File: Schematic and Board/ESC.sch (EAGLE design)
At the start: 45 parts

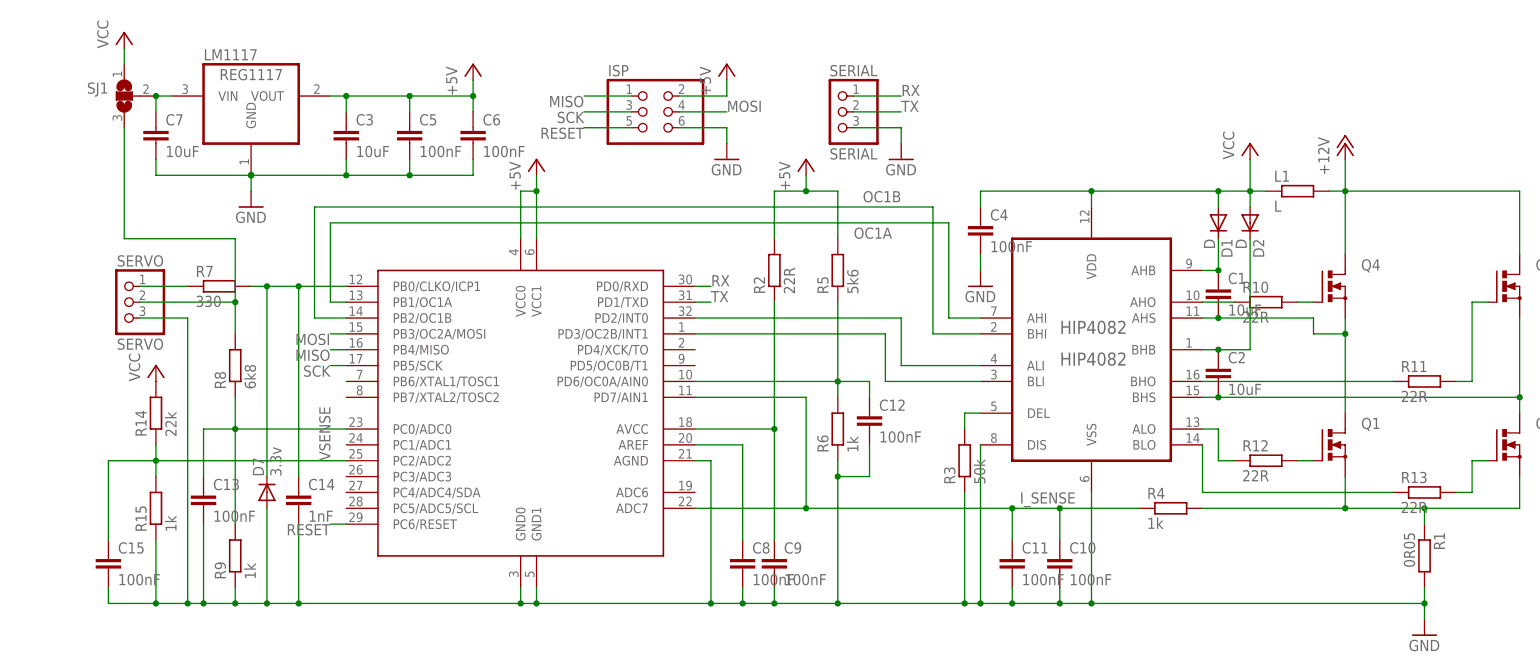
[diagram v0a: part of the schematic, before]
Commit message: updated board: makes better use of PWM outputs, also adds optional ACS712 hall effect current sensor
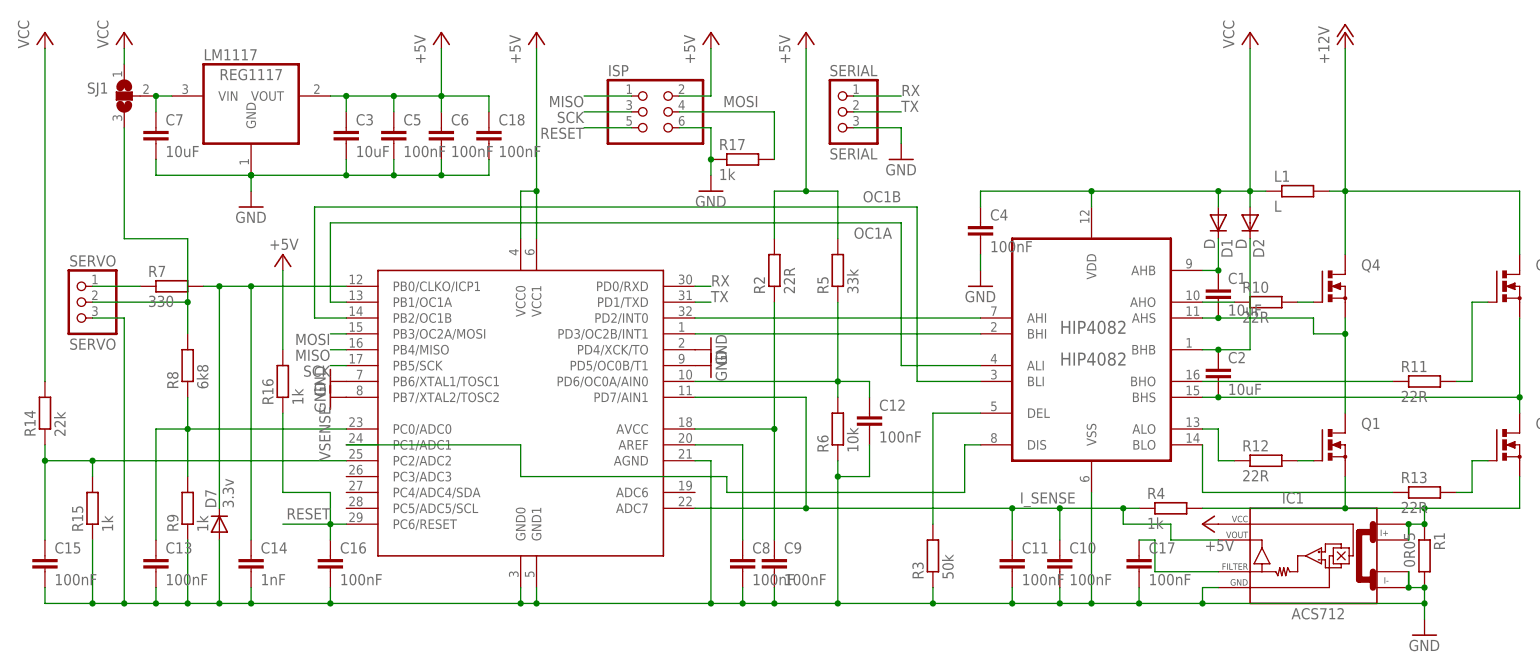
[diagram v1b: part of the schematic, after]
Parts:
- added C16, C17, C18: 100nF, rcl:C-EUC0603K
- added IC1: ACS712, ACS712:ACS712
- added R16, R17: 1k, rcl:R-EU_R0603
- R2, R3, R4, R8, R9: device rcl:R-EU_R0805 -> rcl:R-EU_R0603
- R5: value 5k6 -> 33k; device rcl:R-EU_R0805 -> rcl:R-EU_R0603
- R6: value 1k -> 10k; device rcl:R-EU_R0805 -> rcl:R-EU_R0603
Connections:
- new net AHI: ATMEGA328.PD2/INT0, HIP4082.AHI
- new net BHI: ATMEGA328.PD3/OC2B/INT1, HIP4082.BHI
- net +5V: now also C18.1, IC1.VCC, R16.2
- net GND: now also ATMEGA328.PB6/XTAL1/TOSC1, ATMEGA328.PB7/XTAL2/TOSC2, ATMEGA328.PD4/XCK/TO, ATMEGA328.PD5/OC0B/T1, C16.2, C17.2, C18.2, IC1.GND, IC1.I-_0, IC1.I-_1, R17.1; no longer HIP4082.DIS
- net I_SENSE: now also IC1.VOUT
- net MOSI: now also R17.2
- net N$14: now also ATMEGA328.PC1/ADC1, HIP4082.DIS; no longer ATMEGA328.PD2/INT0, HIP4082.ALI
- net N$15: now also C17.1, IC1.FILTER; no longer ATMEGA328.PD3/OC2B/INT1, HIP4082.BLI
- net OC1A: now also HIP4082.ALI; no longer HIP4082.AHI
- net OC1B: now also HIP4082.BLI; no longer HIP4082.BHI
- net RESET: now also C16.1, R16.1
- net SENSE: now also IC1.I+_0, IC1.I+_1
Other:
- moved on the sheet: C13, C14, C15, C5, C6, D7, R14, R15, R3, R7, R8, R9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

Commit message: 24V adaption - add 7812, expand board, add VMM capacitors, add encoder input.
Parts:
- removed L1: L, rcl:R-EU_M0805
- added C19, C20: 100uF, rcl:CPOL-USD
- added ENC: ENC, pinhead:PINHD-1X3
- added IC2: 78L12F, linear:78L12F
- R14: value 22k -> 33k
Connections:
- net N$14 renamed DISABLE
- net N$4 renamed SERVO_IN
- new net N$19: ATMEGA328.PD4/XCK/TO, ENC.1
- new net N$22: ATMEGA328.PD5/OC0B/T1, ENC.2
- net +12V: now also C4.1, D1.A, D2.A, HIP4082.VDD, IC2.VO, SJ1.1; no longer L1.2, Q3.D, Q4.D
- net GND: now also C19.-, C20.-, ENC.3, IC2.GND, IC2.GND@1; no longer ATMEGA328.PB6/XTAL1/TOSC1, ATMEGA328.PB7/XTAL2/TOSC2, ATMEGA328.PD4/XCK/TO, ATMEGA328.PD5/OC0B/T1
- net VCC: now also C19.+, C20.+, IC2.VI, Q3.D, Q4.D; no longer C4.1, D1.A, D2.A, HIP4082.VDD, L1.1, SJ1.1
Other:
- moved on the sheet: C1, C10, C11, C12, C13, C14, C15, C16, C17, C2, C4, D1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

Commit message: Minor tidying
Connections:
- net N$23 renamed SERVO_VSENSE
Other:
- moved on the sheet: C1, C10, C11, C17, C19, C2, C20, C4, D1, D2, HIP4082, IC1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

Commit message: More board tweaks
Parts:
- added C21: 100nF, rcl:C-EUC0603K
- Q1, Q2, Q3, Q4: value (none) -> IRL1404Z
- R1: value 0R05 -> 0R005
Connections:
- net +12V: now also C21.1
- net GND: now also C21.2
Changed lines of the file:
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@@
 </classes>
 <parts>
-<part name="Q1" library="transistor-power" deviceset="PMOSFET_N" device="TO220BV"/>
-<part name="Q2" library="transistor-power" deviceset="PMOSFET_N" device="TO220BV"/>
-<part name="Q3" library="transistor-power" deviceset="PMOSFET_N" device="TO220BV"/>
-<part name="Q4" library="transistor-power" deviceset="PMOSFET_N" device="TO220BV"/>
+<part name="Q1" library="transistor-power" deviceset="PMOSFET_N" device="TO220BV" value="IRL1404Z"/>
+<part name="Q2" library="transistor-power" deviceset="PMOSFET_N" device="TO220BV" value="IRL1404Z"/>
+<part name="Q3" library="transistor-power" deviceset="PMOSFET_N" device="TO220BV" value="IRL1404Z"/>
+<part name="Q4" library="transistor-power" deviceset="PMOSFET_N" device="TO220BV" value="IRL1404Z"/>
 <part name="GND1" library="supply1" deviceset="GND" device=""/>
 <part name="HIP4082" library="HIP4082" deviceset="HIP4082IBZ" device="" value="HIP4082"/>
@@
 <part name="LM1117" library="burr-brown" deviceset="REG1117" device=""/>
 <part name="P+2" library="supply1" deviceset="+5V" device=""/>
-<part name="R1" library="rcl" deviceset="R-EU_" device="R2512" value="0R05"/>
+<part name="R1" library="rcl" deviceset="R-EU_" device="R2512" value="0R005"/>
 <part name="C3" library="rcl" deviceset="C-EU" device="C0805K" value="10uF"/>
 <part name="C4" library="rcl" deviceset="C-EU" device="C0603K" value="100nF"/>
@@
 <part name="GND9" library="supply1" deviceset="GND" device=""/>
 <part name="GND11" library="supply1" deviceset="GND" device=""/>
+<part name="C21" library="rcl" deviceset="C-EU" device="C0603K" value="100nF"/>
+<part name="GND12" library="supply1" deviceset="GND" device=""/>
 </parts>
 <sheets>
@@
 <instance part="GND3" gate="1" x="-109.22" y="81.28"/>
 <instance part="P+3" gate="VCC" x="106.68" y="109.22"/>
-<instance part="GND2" gate="1" x="40.64" y="68.58"/>
+<instance part="GND2" gate="1" x="40.64" y="71.12"/>
 <instance part="P+4" gate="1" x="-63.5" y="109.22"/>
 <instance part="P+5" gate="1" x="-20.32" y="109.22"/>
@@
 <instance part="GND9" gate="1" x="-149.86" y="12.7"/>
 <instance part="GND11" gate="1" x="-190.5" y="12.7"/>
+<instance part="C21" gate="G$1" x="33.02" y="78.74"/>
+<instance part="GND12" gate="1" x="33.02" y="71.12"/>
 </instances>
 <busses>
@@
 <pinref part="GND2" gate="1" pin="GND"/>
 <pinref part="C4" gate="G$1" pin="2"/>
-<wire x1="40.64" y1="73.66" x2="40.64" y2="71.12" width="0.1524" layer="91"/>
 </segment>
 <segment>
@@
 <junction x="-190.5" y="17.78"/>
 </segment>
+<segment>
+<pinref part="C21" gate="G$1" pin="2"/>
+<pinref part="GND12" gate="1" pin="GND"/>
+</segment>
 </net>
 <net name="N$1" class="0">
@@
 <pinref part="P+1" gate="1" pin="+12V"/>
 <wire x1="83.82" y1="83.82" x2="83.82" y2="106.68" width="0.1524" layer="91"/>
-</segment>
-<segment>
+<pinref part="C21" gate="G$1" pin="1"/>
+<wire x1="40.64" y1="83.82" x2="33.02" y2="83.82" width="0.1524" layer="91"/>
+<wire x1="33.02" y1="83.82" x2="33.02" y2="81.28" width="0.1524" layer="91"/>
+<junction x="40.64" y="83.82"/>
+</segment>
+<segment>

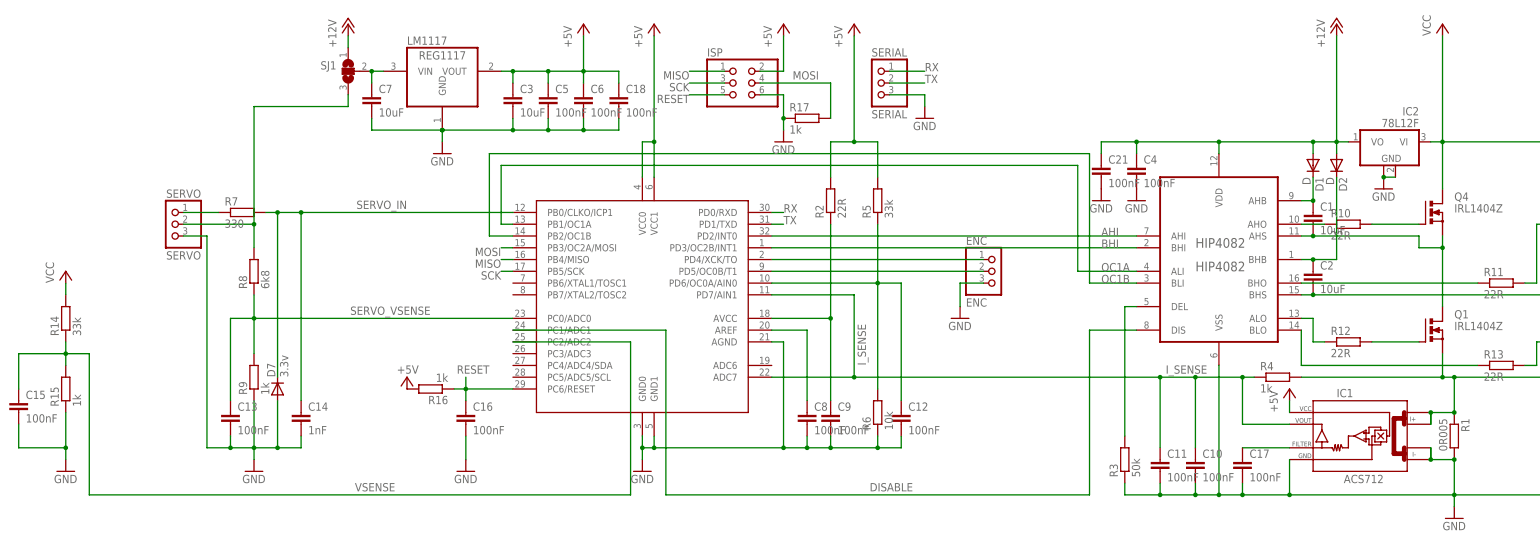
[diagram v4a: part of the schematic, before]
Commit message: Remove ACS712, improve ground stitching and layout
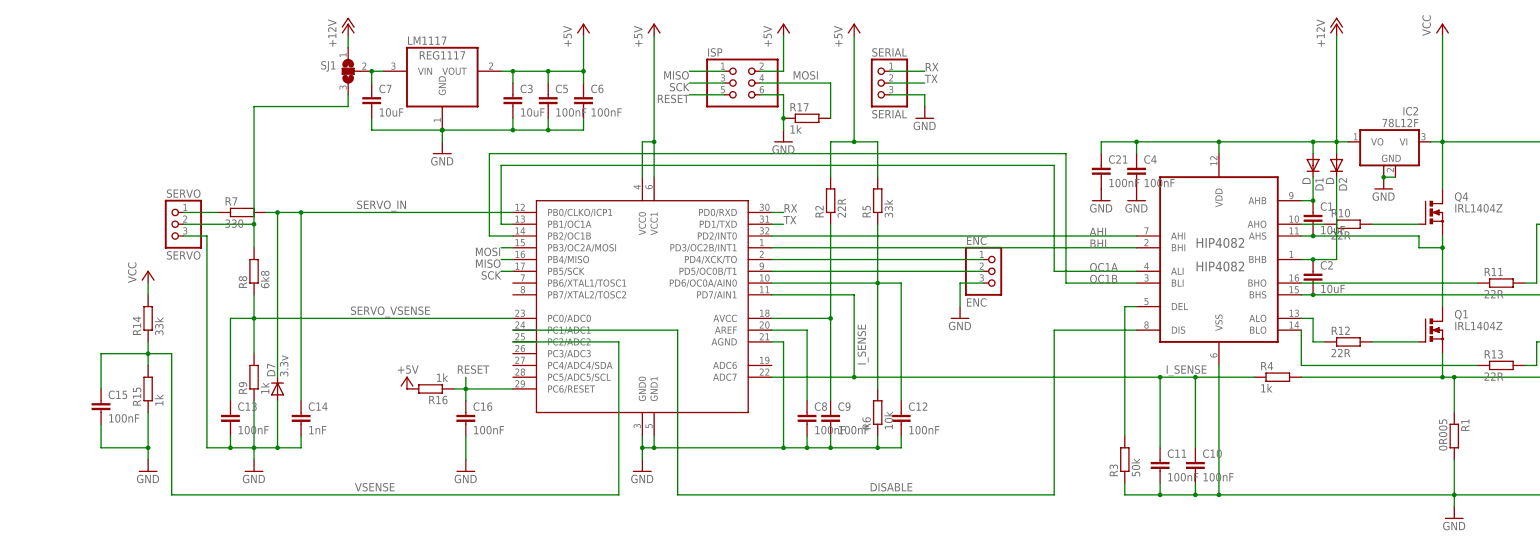
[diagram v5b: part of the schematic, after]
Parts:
- removed C17, C18: 100nF, rcl:C-EUC0603K
- removed IC1: ACS712, ACS712:ACS712
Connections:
- removed net N$15: C17.1, IC1.FILTER
- net +5V: no longer C18.1, IC1.VCC
- net GND: no longer C17.2, C18.2, IC1.GND, IC1.I-_0, IC1.I-_1
- net I_SENSE: no longer IC1.VOUT
- net SENSE: no longer IC1.I+_0, IC1.I+_1
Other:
- moved on the sheet: C15, R14, R15
